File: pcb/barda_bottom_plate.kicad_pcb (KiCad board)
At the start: 2 copper layers, 228.6 x 76.2 mm, 2 parts

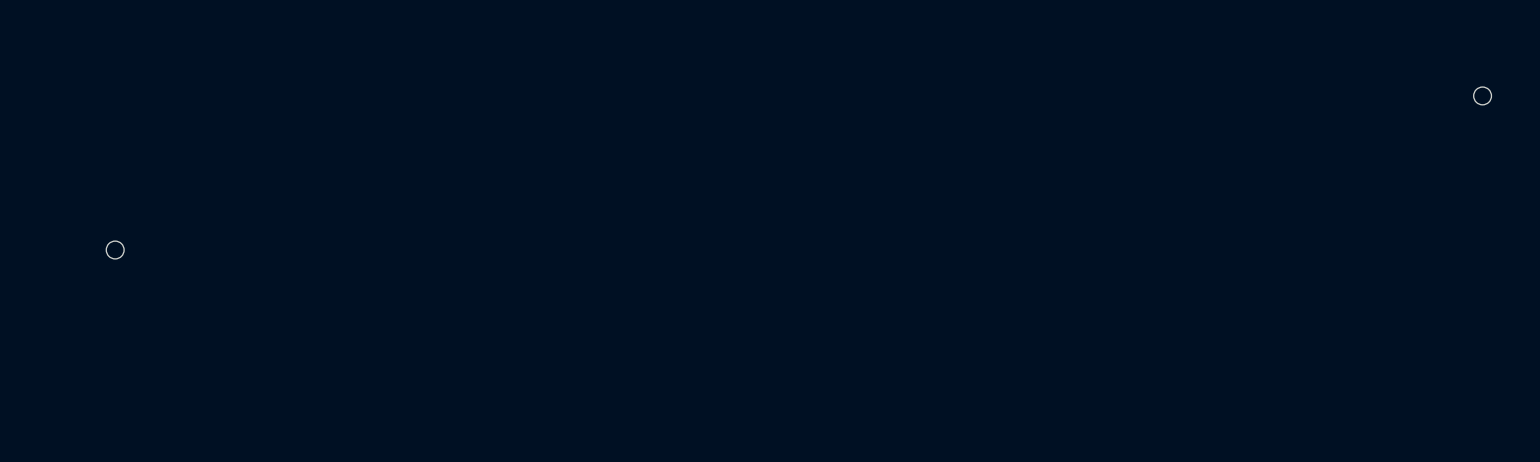
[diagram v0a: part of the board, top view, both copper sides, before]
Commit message: Add case 3D models and update PCB assets
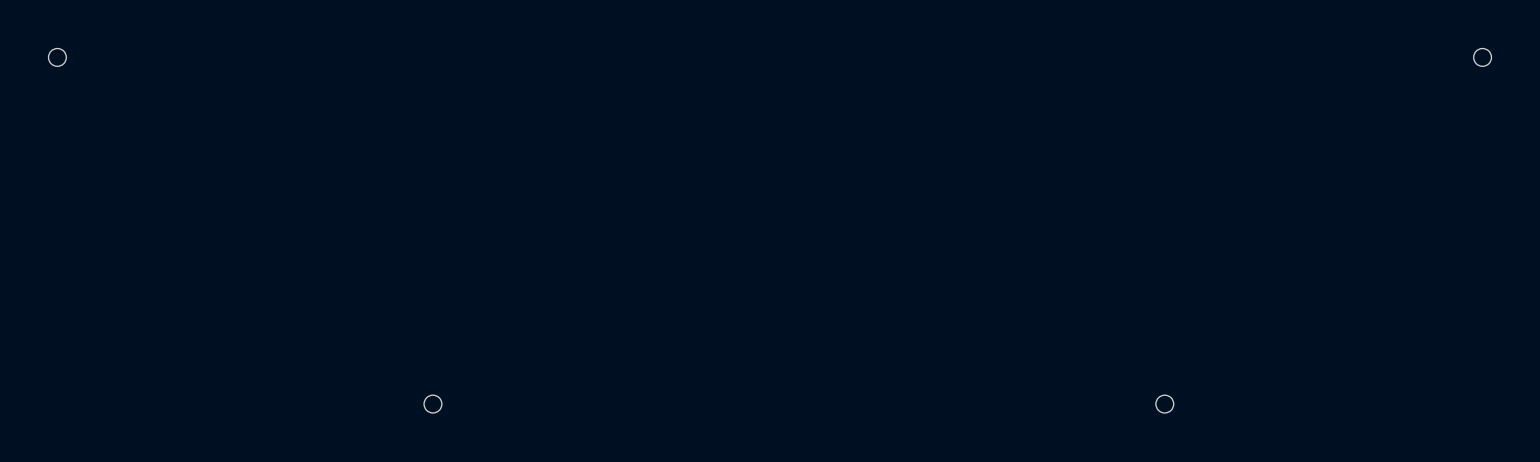
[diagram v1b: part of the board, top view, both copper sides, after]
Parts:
- removed the REF** at (39.3, 66.7)
- added REF**: MountingHole_2.2mm_M2, MountingHole:MountingHole_2.2mm_M2, F.Cu at (32.1, 42.9)
- added REF**: MountingHole_2.2mm_M2, MountingHole:MountingHole_2.2mm_M2, F.Cu at (169.1, 85.7)
- added REF**: MountingHole_2.2mm_M2, MountingHole:MountingHole_2.2mm_M2, F.Cu at (78.6, 85.7)
- moved REF** 4.76 mm to (208.4, 42.9)
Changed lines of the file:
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@@
 	(generator_version "10.0")
 	(general
-		(thickness 1.6)
+		(thickness 1.29)
 		(legacy_teardrops no)
 	)
@@
 	)
 	(setup
+		(stackup
+			(layer "F.SilkS"
+				(type "Top Silk Screen")
+			)
+			(layer "F.Paste"
+				(type "Top Solder Paste")
+			)
+			(layer "F.Mask"
+				(type "Top Solder Mask")
+				(thickness 0.01)
+			)
+			(layer "F.Cu"
+				(type "copper")
+				(thickness 0.035)
+			)
+			(layer "dielectric 1"
+				(type "core")
+				(thickness 1.2)
+				(material "FR4")
+				(epsilon_r 4.5)
+				(loss_tangent 0.02)
+			)
+			(layer "B.Cu"
+				(type "copper")
+				(thickness 0.035)
+			)
+			(layer "B.Mask"
+				(type "Bottom Solder Mask")
+				(thickness 0.01)
+			)
+			(layer "B.Paste"
+				(type "Bottom Solder Paste")
+			)
+			(layer "B.SilkS"
+				(type "Bottom Silk Screen")
+			)
+			(copper_finish "None")
+			(dielectric_constraints no)
+		)
 		(pad_to_mask_clearance 0)
 		(allow_soldermask_bridges_in_footprints no)
@@
 	(footprint "MountingHole:MountingHole_2.2mm_M2"
 		(layer "F.Cu")
-		(at 39.290625 66.675)
+		(at 32.146875 42.8625)
 		(descr "Mounting Hole 2.2mm, M2, no annular, generated by kicad-footprint-generator mountinghole.py")
 		(tags "mountinghole M2")
@@
 	(footprint "MountingHole:MountingHole_2.2mm_M2"
 		(layer "F.Cu")
-		(at 208.359375 47.625)
+		(at 169.06875 85.725)
 		(descr "Mounting Hole 2.2mm, M2, no annular, generated by kicad-footprint-generator mountinghole.py")
 		(tags "mountinghole M2")
+		(property "Reference" "REF**"
+			(at 0 -3.15 0)
+			(layer "F.SilkS")
+			(hide yes)
+			(effects
+				(font
+					(size 1 1)
+					(thickness 0.15)
+				)
+			)
+		)
+		(property "Value" "MountingHole_2.2mm_M2"
+			(at 0 3.15 0)
+			(layer "F.Fab")
+			(effects
+				(font
+					(size 1 1)
+					(thickness 0.15)
+				)
+			)
+		)
+		(property "Datasheet" ""
+			(at 0 0 0)
+			(layer "F.Fab")
+			(hide yes)
+			(effects
+				(font
+					(size 1.27 1.27)
+				)
+			)
+		)
+		(property "Description" ""
+			(at 0 0 0)
+			(layer "F.Fab")
+			(hide yes)
+			(effects
+				(font
+					(size 1.27 1.27)
+				)
+			)
+		)
+		(property "KiLib_Generator" "mounting_hardware/mounting_hole"
+			(at 0 0 0)
+			(layer "F.SilkS")
+			(hide yes)
+			(effects
+				(font
+					(size 1 1)
+					(thickness 0.15)
+				)
+			)
+		)
+		(attr exclude_from_pos_files exclude_from_bom)
+		(duplicate_pad_numbers_are_jumpers no)
+		(fp_circle
+			(center 0 0)
+			(end 2.2 0)
+			(stroke
+				(width 0.15)
+				(type solid)
+			)
+			(fill no)
+			(layer "Cmts.User")
+		)
+		(fp_circle
+			(center 0 0)
+			(end 2.45 0)
+			(stroke
+				(width 0.05)
+				(type solid)
+			)
+			(fill no)
+			(layer "F.CrtYd")
+		)
+		(fp_text user "${REFERENCE}"
+			(at 0 0 0)
+			(layer "F.Fab")
+			(effects
+				(font
+					(size 1 1)
+					(thickness 0.15)
+				)
+			)
+		)
+		(pad "" np_thru_hole circle
+			(at 0 0)
+			(size 2.2 2.2)
+			(drill 2.2)
+			(layers "*.Cu" "*.Mask")
+		)
+		(embedded_fonts no)
+	)
+	(footprint "MountingHole:MountingHole_2.2mm_M2"
+		(layer "F.Cu")
+		(at 78.58125 85.725)
+		(descr "Mounting Hole 2.2mm, M2, no annular, generated by kicad-footprint-generator mountinghole.py")
+		(tags "mountinghole M2")
+		(property "Reference" "REF**"
+			(at 0 -3.15 0)
+			(layer "F.SilkS")
+			(hide yes)
+			(effects
+				(font
+					(size 1 1)
+					(thickness 0.15)
+				)
+			)
+		)
+		(property "Value" "MountingHole_2.2mm_M2"
+			(at 0 3.15 0)
+			(layer "F.Fab")
+			(effects
+				(font
+					(size 1 1)
+					(thickness 0.15)
+				)
+			)
+		)
+		(property "Datasheet" ""
+			(at 0 0 0)
+			(layer "F.Fab")
+			(hide yes)
+			(effects
+				(font
+					(size 1.27 1.27)
+				)
+			)
+		)
+		(property "Description" ""
+			(at 0 0 0)
+			(layer "F.Fab")
+			(hide yes)
+			(effects
+				(font
+					(size 1.27 1.27)
+				)
+			)
+		)
+		(property "KiLib_Generator" "mounting_hardware/mounting_hole"
+			(at 0 0 0)
+			(layer "F.SilkS")
+			(hide yes)
+			(effects
+				(font
+					(size 1 1)
+					(thickness 0.15)
+				)
+			)
+		)
+		(attr exclude_from_pos_files exclude_from_bom)
+		(duplicate_pad_numbers_are_jumpers no)
+		(fp_circle
+			(center 0 0)
+			(end 2.2 0)
+			(stroke
+				(width 0.15)
+				(type solid)
+			)
+			(fill no)
+			(layer "Cmts.User")
+		)
+		(fp_circle
+			(center 0 0)
+			(end 2.45 0)
+			(stroke
+				(width 0.05)
+				(type solid)
+			)
+			(fill no)
+			(layer "F.CrtYd")
+		)
+		(fp_text user "${REFERENCE}"
+			(at 0 0 0)
+			(layer "F.Fab")
+			(effects
+				(font
+					(size 1 1)
+					(thickness 0.15)
+				)
+			)
+		)
+		(pad "" np_thru_hole circle
+			(at 0 0)
+			(size 2.2 2.2)
+			(drill 2.2)
+			(layers "*.Cu" "*.Mask")
+		)
+		(embedded_fonts no)
+	)
+	(footprint "MountingHole:MountingHole_2.2mm_M2"
+		(layer "F.Cu")
+		(at 208.359375 42.8625)
+		(descr "Mounting Hole 2.2mm, M2, no annular, generated by kicad-footprint-generator mountinghole.py")
+		(tags "mountinghole M2")

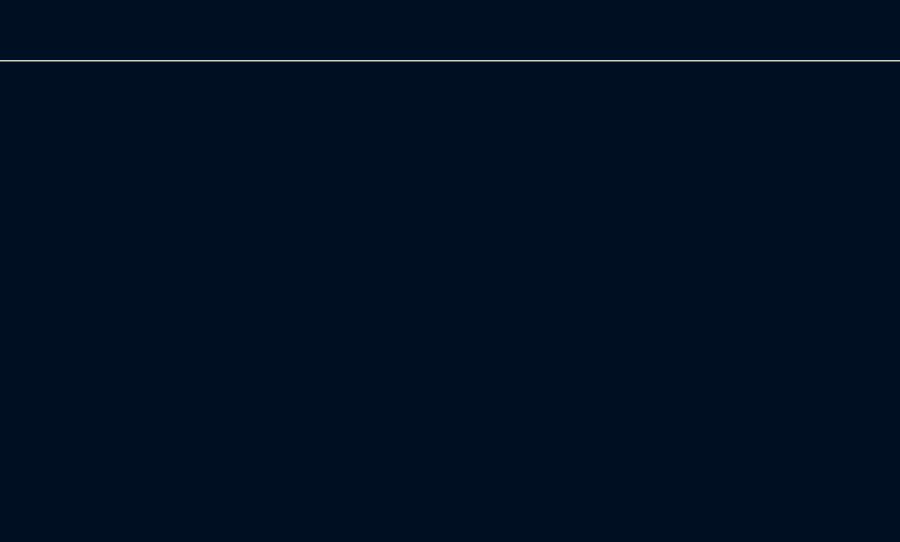
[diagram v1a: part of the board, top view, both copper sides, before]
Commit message: Update Barda case and PCB design
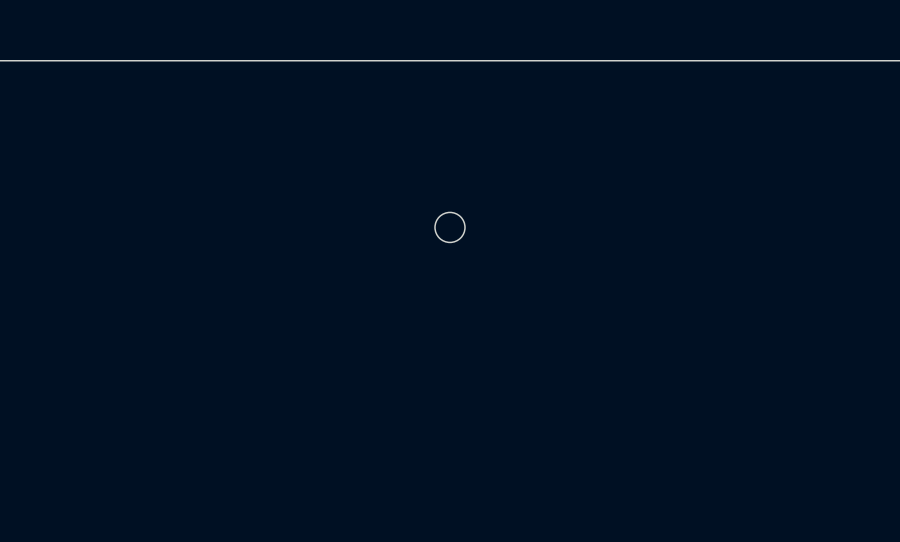
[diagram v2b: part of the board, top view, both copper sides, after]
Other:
- outline, holes or cut-outs redrawn
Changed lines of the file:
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@@
+		(layer "Edge.Cuts")
+	)
+	(gr_circle
+		(center 123.825 24.60625)
+		(end 124.325 24.60625)
+		(stroke
+			(width 0.05)
+			(type solid)
+		)
+		(fill no)
 		(layer "Edge.Cuts")
 	)

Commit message: Update PCB and case for M2 4mm standoffs
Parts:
- added BT1: CR2032, Smidr:BAT-SMD_MY-1632-03, F.Cu at (206.4, 176.2)
- added TP1: +BATT, TestPoint:TestPoint_Keystone_5019_Miniature, F.Cu at (201.6, 133.3)
- added TP2: -BATT, TestPoint:TestPoint_Keystone_5019_Miniature, F.Cu at (206.4, 133.3)
- moved REF** 120.9 mm to (249.2, 176.2)
- moved REF** 120.9 mm to (158.8, 176.2)
- moved REF** 120.9 mm to (112.3, 133.3)
- moved REF** 120.9 mm to (288.5, 133.3)
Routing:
- net +BATT: track 0.00 -> 69.2 mm
- net GND: track 0.00 -> 45.0 mm
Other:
- outline, holes or cut-outs redrawn

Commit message: Update Barda case and PCB designs
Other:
- outline, holes or cut-outs redrawn
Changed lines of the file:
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@@
 		(capping no)
 		(filling no)
-		(zone_defaults)
 		(pcbplotparams
 			(layerselection 0x00000000_00000000_55555555_5755f5ff)
@@
 		)
 		(property "Value" "CR2032"
-			(at 0 8.365625 0)
+			(at 0.00052 6.152022 0)
 			(layer "F.SilkS")
 			(effects
@@
 			(mid -6.354329 5.885117)
 			(end -8.00057 3.423876)
-			(stroke
-				(width 0.25)
-				(type solid)
-			)
-			(layer "F.SilkS")
-		)
-		(fp_arc
-			(start -3.43 6.35)
-			(mid -0.000308 4.926313)
-			(end 3.429565 6.349564)
 			(stroke
 				(width 0.25)
@@
 	)
 	(gr_line
-		(start 89.69375 111.91875)
-		(end 89.69375 183.35625)
+		(start 89.69375 111.125)
+		(end 89.69375 184.15)
 		(stroke
 			(width 0.05)
@@
 	)
 	(gr_arc
-		(start 89.69375 111.91875)
-		(mid 90.391202 110.234952)
-		(end 92.075 109.5375)
+		(start 89.69375 111.125)
+		(mid 90.158718 110.002468)
+		(end 91.28125 109.5375)
 		(stroke
 			(width 0.05)
@@
 	)
 	(gr_arc
-		(start 92.075 185.7375)
-		(mid 90.391202 185.040048)
-		(end 89.69375 183.35625)
+		(start 91.28125 185.7375)
+		(mid 90.158718 185.272532)
+		(end 89.69375 184.15)
 		(stroke
 			(width 0.05)
@@
 	)
 	(gr_line
-		(start 92.075 185.7375)
-		(end 315.9125 185.7375)
+		(start 91.28125 185.7375)
+		(end 194.304359 185.7375)
+		(stroke
+			(width 0.05)
+			(type default)
+		)
+		(layer "Edge.Cuts")
+	)
+	(gr_arc
+		(start 194.584992 185.621258)
+		(mid 194.456235 185.707285)
+		(end 194.304359 185.7375)
+		(stroke
+			(width 0.05)
+			(type default)
+		)
+		(layer "Edge.Cuts")
+	)
+	(gr_line
+		(start 194.584992 185.621258)
+		(end 196.675179 183.531071)
+		(stroke
+			(width 0.05)
+			(type default)
+		)
+		(layer "Edge.Cuts")
+	)
+	(gr_arc
+		(start 196.675179 183.531071)
+		(mid 196.868817 183.401671)
+		(end 197.097235 183.35625)
+		(stroke
+			(width 0.05)
+			(type default)
+		)
+		(layer "Edge.Cuts")
+	)
+	(gr_line
+		(start 197.097235 183.35625)
+		(end 215.652767 183.35625)
 		(stroke
 			(width 0.05)
@@
 		(layer "Edge.Cuts")
 	)
+	(gr_arc
+		(start 215.652767 183.35625)
+		(mid 215.881181 183.401685)
+		(end 216.07482 183.531072)
+		(stroke
+			(width 0.05)
+			(type default)
+		)
+		(layer "Edge.Cuts")
+	)
 	(gr_line
-		(start 315.9125 109.5375)
-		(end 92.075 109.5375)
+		(start 216.07482 183.531072)
+		(end 218.165009 185.621258)
 		(stroke
 			(width 0.05)
@@
 	)
 	(gr_arc
-		(start 315.9125 109.5375)
-		(mid 317.596283 110.234967)
-		(end 318.29375 111.91875)
+		(start 218.445642 185.7375)
+		(mid 218.293764 185.70729)
+		(end 218.165009 185.621258)
+		(stroke
+			(width 0.05)
+			(type default)
+		)
+		(layer "Edge.Cuts")
+	)
+	(gr_line
+		(start 218.445642 185.7375)
+		(end 316.70625 185.7375)
+		(stroke
+			(width 0.05)
+			(type default)
+		)
+		(layer "Edge.Cuts")
+	)
+	(gr_line
+		(start 316.70625 109.5375)
+		(end 91.28125 109.5375)
 		(stroke
 			(width 0.05)
@@
 	)
 	(gr_arc
-		(start 318.29375 183.35625)
-		(mid 317.596283 185.040033)
-		(end 315.9125 185.7375)
+		(start 316.70625 109.5375)
+		(mid 317.828782 110.002468)
+		(end 318.29375 111.125)
+		(stroke
+			(width 0.05)
+			(type default)
+		)
+		(layer "Edge.Cuts")
+	)
+	(gr_arc
+		(start 318.29375 184.15)
+		(mid 317.828782 185.272532)
+		(end 316.70625 185.7375)
 		(stroke
 			(width 0.05)
@@
 	)
 	(gr_line
-		(start 318.293749 183.35625)
-		(end 318.29375 111.91875)
-		(stroke
-			(width 0.05)
+		(start 318.29375 184.15)
+		(end 318.29375 111.125)
+		(stroke
+			(width 0.05)
